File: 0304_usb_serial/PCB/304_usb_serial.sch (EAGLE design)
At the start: 20 parts, among them IC1 FT231XQ

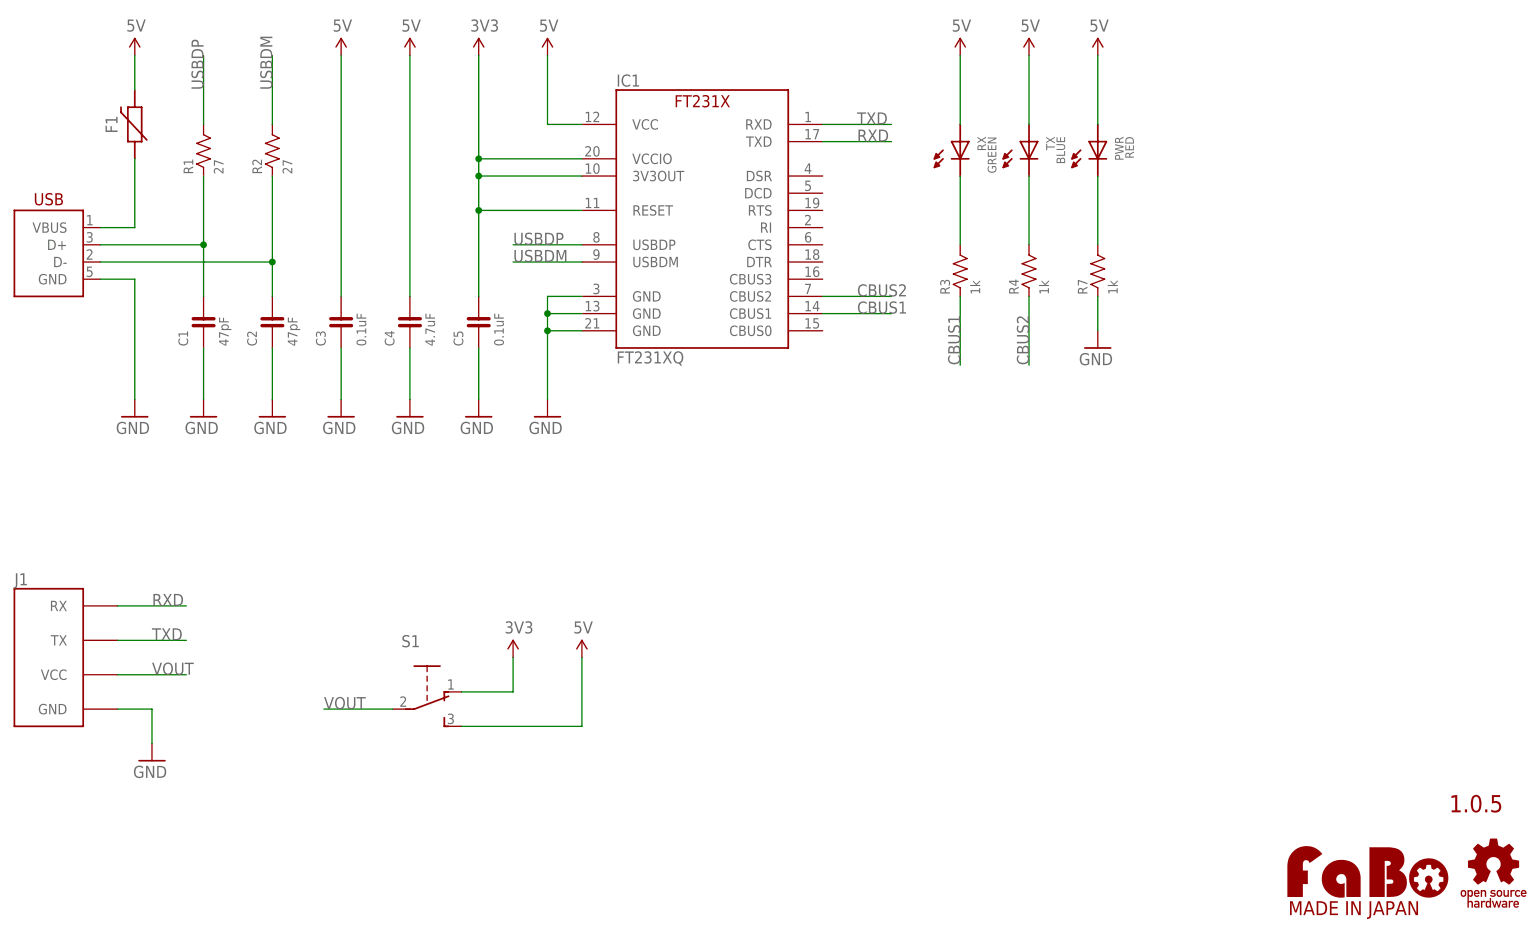
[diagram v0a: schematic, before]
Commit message: #303 phonejack　ロゴ修正　#304 usb_serial　ロゴ修正
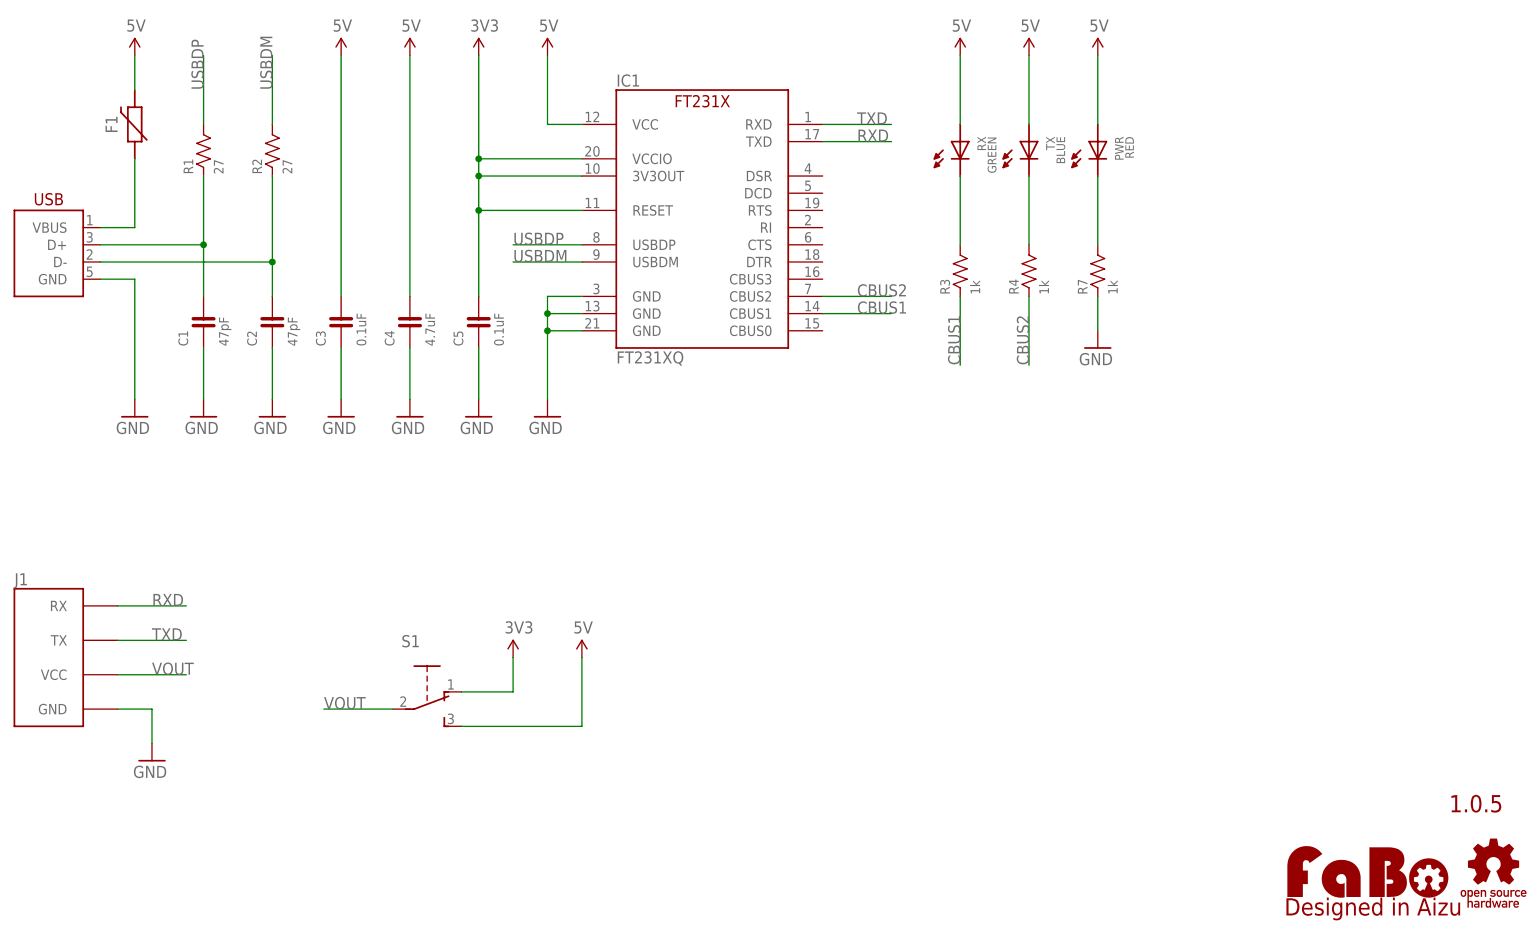
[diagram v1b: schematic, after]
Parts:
- removed U$2: (no value), FaBo-Logo:LOGO_FABO-M_BOTTOM
- added LOGO1: (no value), component:LOGO_FABO-M_BOTTOM
